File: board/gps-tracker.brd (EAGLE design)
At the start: 52.1 x 77.5 mm, 30 parts, among them J2 AVR_SPI_PRG_6OFFSET_PADS, U2 MCP73831, U3 ATMEGA328P, X1 USBSMD

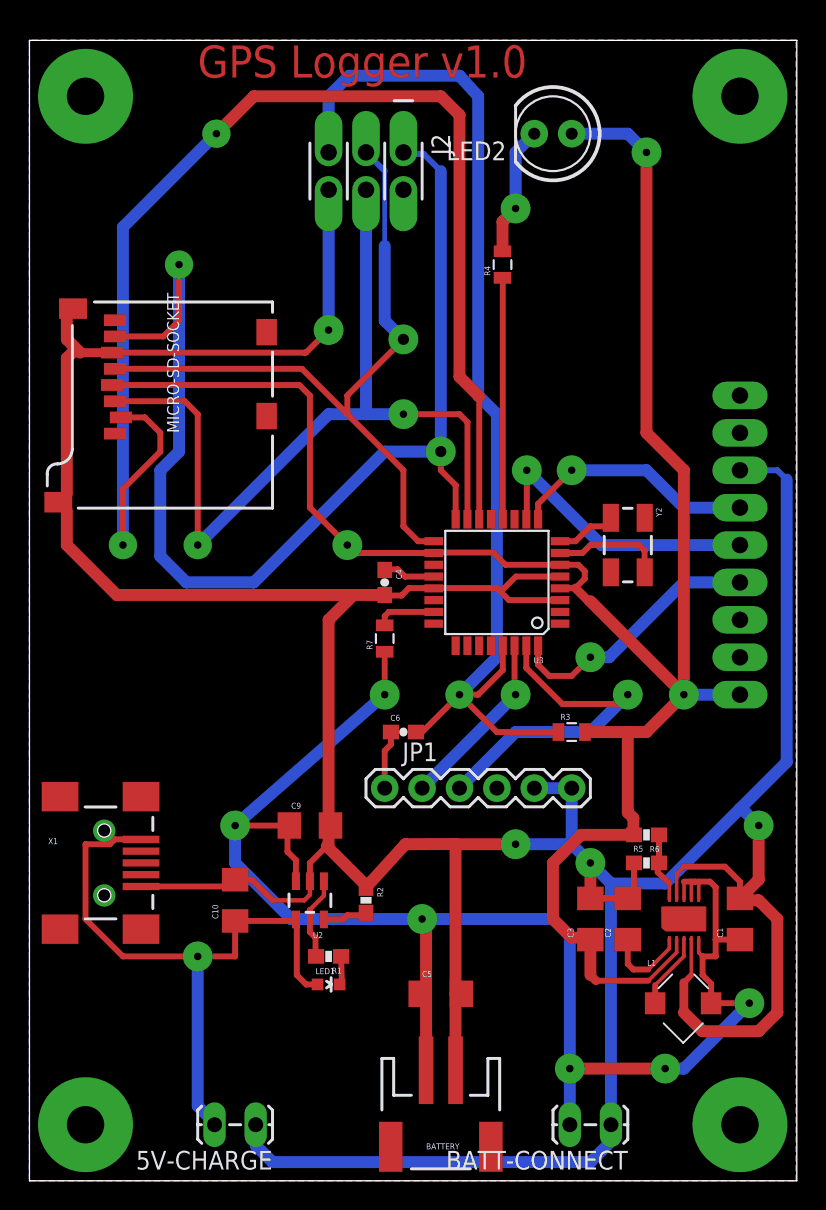
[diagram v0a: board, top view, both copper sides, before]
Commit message: Updating board to correct for previous errors, adding another status LED and bringing out the GPS EN pin to the arduino
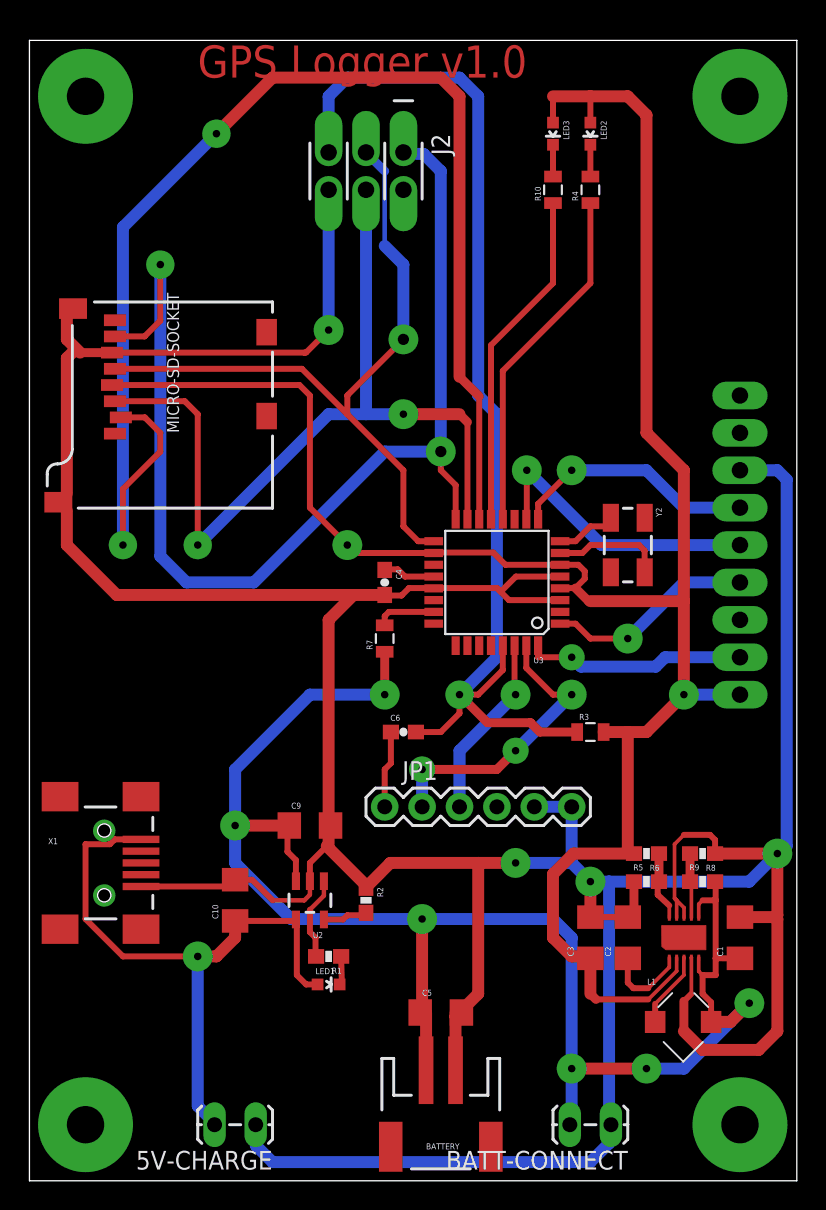
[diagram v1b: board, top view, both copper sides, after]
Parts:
- added LED3: (no value), SparkFun-LED:LED-0603
- added R10: 150, SparkFun:0805
- added R8: 47k, SparkFun:0603-RES
- added R9: 470k, SparkFun:0603-RES
- LED2: device SparkFun-LED:LED5MM -> SparkFun-LED:LED-0603
- moved R4 7.84 mm to (38.1, 67.3)
- moved LED2 2.54 mm to (38.1, 71.1)
- moved JP1 1.27 mm to (24.1, 25.4)
- moved R3 1.27 mm to (38.1, 30.5)
- moved C1 1.27 mm to (48.3, 16.5)
- moved C2 1.27 mm to (40.6, 16.5)
- moved C3 1.27 mm to (38.1, 16.5)
- moved C5 1.27 mm to (27.9, 11.4)
- moved L1 1.27 mm to (44.5, 10.8)
- moved R5 1.27 mm to (41.9, 20.3)
- moved R6 1.27 mm to (41.9, 22.2)
- moved U$1 1.27 mm to (44.5, 16.5)
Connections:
- net BATT_LED renamed STATUS_LED
- removed net EN: GPS-HEADER.2
- new net ALT_STATUS_LED: R10.1, U3.13
- new net GPS_EN: GPS-HEADER.2, U3.32
- new net N$18: LED3.C, R10.2
- new net UVLO: R8.2, R9.1, U$1.7
- net 3.3V: now also LED3.A
- net GND: now also R8.1, U$1.8
- net GPS_FIX: now also U3.1; no longer U3.32
- net N$5: now also LED2.C; no longer LED2.K
- net RXI: now also JP1.RXI; no longer JP1.TXO
- net TXO: now also JP1.TXO; no longer JP1.RXI
- net VBATT: now also R9.2; no longer U$1.7, U$1.8
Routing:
- net ALT_STATUS_LED: track 0.00 -> 23.2 mm
- net GPS_EN: track 0.00 -> 15.0 mm, vias 0 -> 1
- net GND: track 295.7 -> 303.3 mm
- net STATUS_LED: track 16.4 -> 23.9 mm
- net N$5: track 8.88 -> 2.16 mm, vias 1 -> 0
- net 3.3V: track 140.4 -> 145.6 mm, vias 3 -> 2
- net UVLO: track 0.00 -> 4.40 mm
- net GPS_FIX: track 18.0 -> 14.2 mm
- net RXI: track 23.7 -> 20.2 mm, vias 1 -> 3
- net N$18: track 0.00 -> 2.16 mm
- net /RESET: track 74.6 -> 76.4 mm
- net SD_CS: track 88.5 -> 90.3 mm
- net MISO: track 79.5 -> 77.7 mm
- net DTR: track 3.98 -> 5.25 mm
- net VBATT: track 110.1 -> 111.0 mm
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- removed copper zone on layer 1, net N$17
- removed copper zone on layer 16, net N$18
